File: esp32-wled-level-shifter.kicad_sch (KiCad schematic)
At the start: 5 parts, among them J1 Conn_01x04_Female, J2 Conn_01x15_Female, J3 Conn_01x15_Female, U1 CD40106

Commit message: Dimension and size tweaks
- Correctly space connectors
- Increase size of mounting holes, allow M3
- Chamfer board edges
- More silkscreen markings
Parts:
- C1: LCSC (none) -> C14663
- U1: LCSC (none) -> C38184
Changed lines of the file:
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@@
+      (effects (font (size 1.27 1.27)) hide)
+    )
+    (property "LCSC" "C38184" (id 4) (at 34.29 151.13 0)
       (effects (font (size 1.27 1.27)) hide)
     )
@@
       (effects (font (size 1.27 1.27)) hide)
     )
+    (property "LCSC" "C38184" (id 4) (at 34.29 151.13 0)
+      (effects (font (size 1.27 1.27)) hide)
+    )
     (pin "1")
     (pin "2")
@@
       (effects (font (size 1.27 1.27)) hide)
     )
+    (property "LCSC" "C38184" (id 4) (at 34.29 151.13 0)
+      (effects (font (size 1.27 1.27)) hide)
+    )
     (pin "1")
     (pin "2")
@@
     )
     (property "Datasheet" "https://assets.nexperia.com/documents/data-sheet/HEF40106B.pdf" (id 3) (at 34.29 151.13 0)
+      (effects (font (size 1.27 1.27)) hide)
+    )
+    (property "LCSC" "C38184" (id 4) (at 34.29 151.13 0)
       (effects (font (size 1.27 1.27)) hide)
     )
@@
       (effects (font (size 1.27 1.27)) hide)
     )
+    (property "LCSC" "C38184" (id 4) (at 34.29 151.13 0)
+      (effects (font (size 1.27 1.27)) hide)
+    )
     (pin "1")
     (pin "2")
@@
     )
     (property "Datasheet" "https://assets.nexperia.com/documents/data-sheet/HEF40106B.pdf" (id 3) (at 104.14 45.72 0)
+      (effects (font (size 1.27 1.27)) hide)
+    )
+    (property "LCSC" "C38184" (id 4) (at 34.29 151.13 0)
       (effects (font (size 1.27 1.27)) hide)
     )
@@
       (effects (font (size 1.27 1.27)) hide)
     )
-    (property "LCSC" "" (id 4) (at 54.61 152.4 0)
+    (property "LCSC" "C14663 " (id 4) (at 54.61 152.4 0)
       (effects (font (size 1.27 1.27)) hide)
     )
@@
       (effects (font (size 1.27 1.27)) hide)
     )
+    (property "LCSC" "C38184" (id 4) (at 34.29 151.13 0)
+      (effects (font (size 1.27 1.27)) hide)
+    )

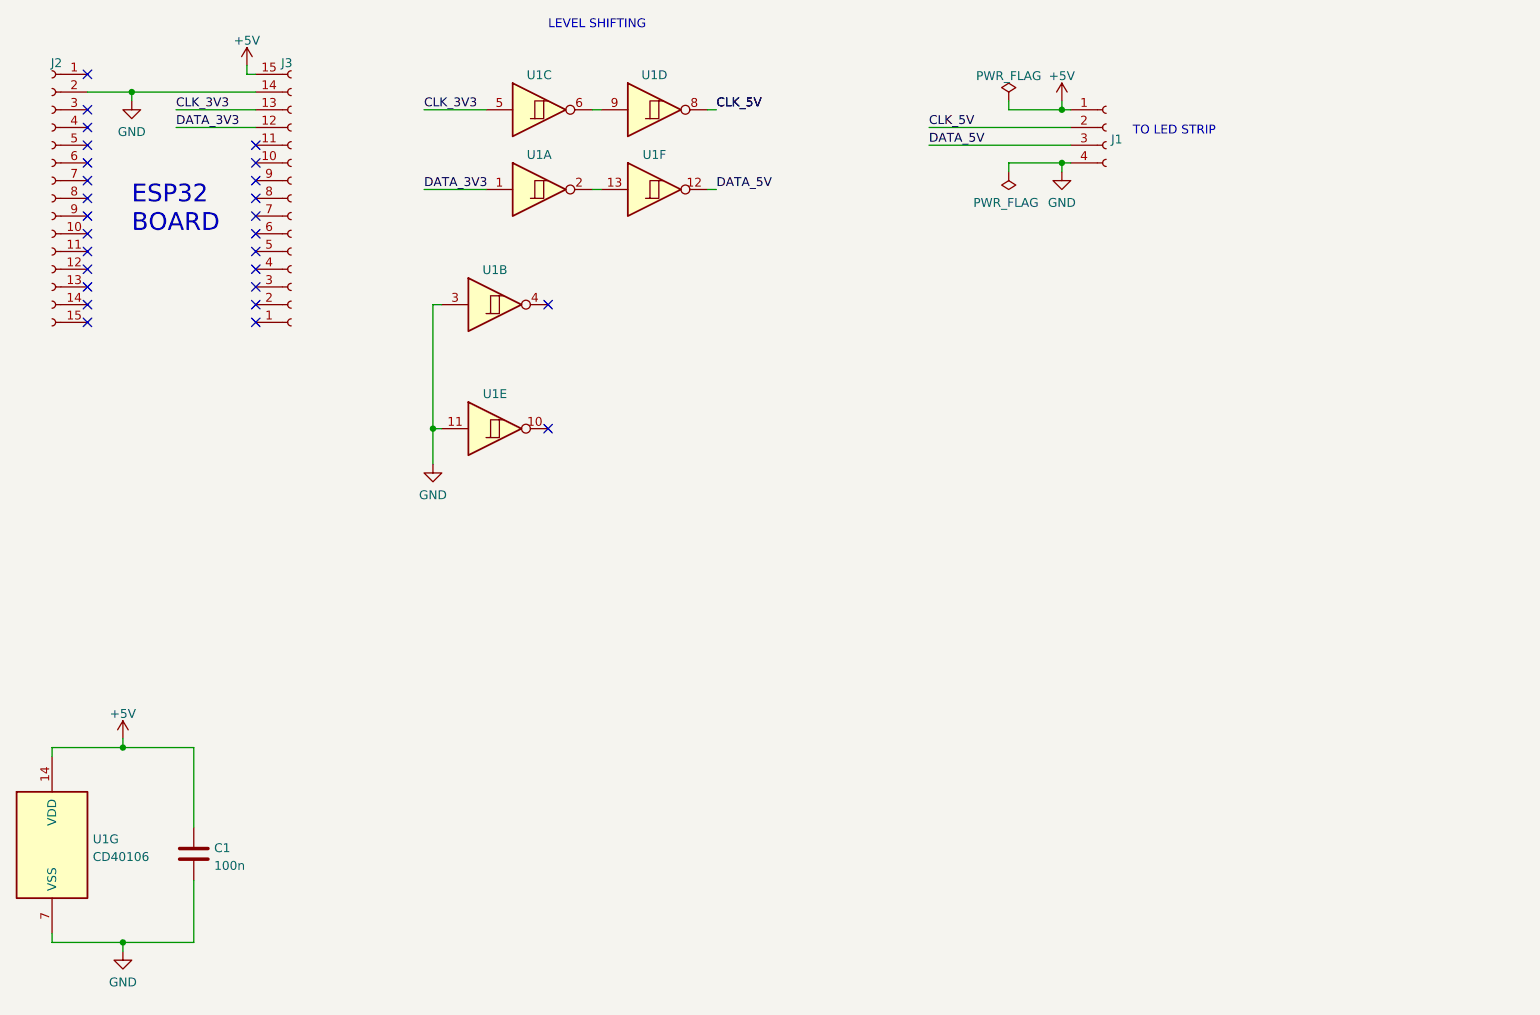
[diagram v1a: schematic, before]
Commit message: Rev2 board with experimenting playground
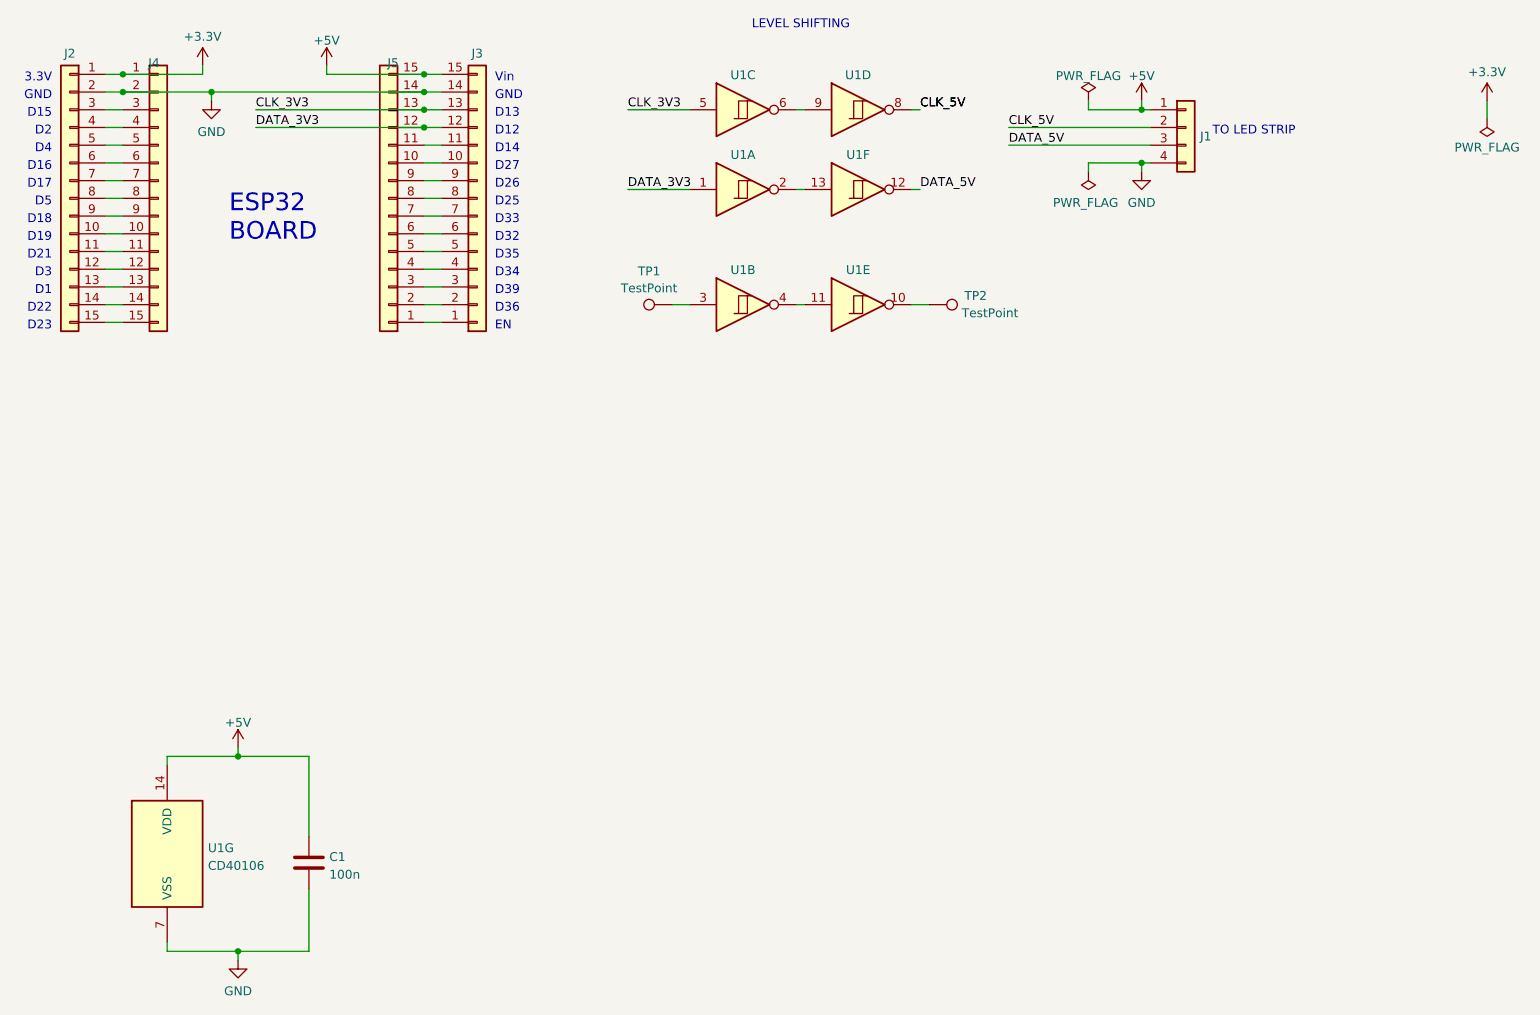
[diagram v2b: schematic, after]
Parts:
- added J4, J5: Conn_01x15_Female, Connector_PinSocket_2.54mm:PinSocket_1x15_P2.54mm_Vertical, symbol Connector_Generic:Conn_01x15
- added TP1, TP2: TestPoint, TestPoint:TestPoint_THTPad_D2.0mm_Drill1.0mm, symbol Connector:TestPoint
- J1: symbol Connector:Conn_01x04_Female -> Connector_Generic:Conn_01x04
- J2, J3: symbol Connector:Conn_01x15_Female -> Connector_Generic:Conn_01x15
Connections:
- net +5V: now also J5.15 (Pin_15)
- net CLK_3V3: now also J5.13 (Pin_13)
- net DATA_3V3: now also J5.12 (Pin_12)
- net GND: now also J4.2 (Pin_2), J5.14 (Pin_14); no longer U1.11, U1.3
- net at U1.10: now also TP2.1
- net at U1.4: now also U1.11
- net at J3.1 (Pin_1): now also J5.1 (Pin_1)
- net at J3.10 (Pin_10): now also J5.10 (Pin_10)
- net at J3.11 (Pin_11): now also J5.11 (Pin_11)
- net at J3.2 (Pin_2): now also J5.2 (Pin_2)
- net at J3.3 (Pin_3): now also J5.3 (Pin_3)
- net at J3.4 (Pin_4): now also J5.4 (Pin_4)
- net at J3.5 (Pin_5): now also J5.5 (Pin_5)
- net at J3.6 (Pin_6): now also J5.6 (Pin_6)
- net at J3.7 (Pin_7): now also J5.7 (Pin_7)
- net at J3.8 (Pin_8): now also J5.8 (Pin_8)
- net at J3.9 (Pin_9): now also J5.9 (Pin_9)
- net +3.3V: now reaches J2.1 (Pin_1)
- net +3.3V: now also J4.1 (Pin_1)
- net at J2.10 (Pin_10): now also J4.10 (Pin_10)
- net at J2.11 (Pin_11): now also J4.11 (Pin_11)
- net at J2.12 (Pin_12): now also J4.12 (Pin_12)
- net at J2.13 (Pin_13): now also J4.13 (Pin_13)
- net at J2.14 (Pin_14): now also J4.14 (Pin_14)
- net at J2.15 (Pin_15): now also J4.15 (Pin_15)
- net at J2.3 (Pin_3): now also J4.3 (Pin_3)
- net at J2.4 (Pin_4): now also J4.4 (Pin_4)
- net at J2.5 (Pin_5): now also J4.5 (Pin_5)
- net at J2.6 (Pin_6): now also J4.6 (Pin_6)
- net at J2.7 (Pin_7): now also J4.7 (Pin_7)
- net at J2.8 (Pin_8): now also J4.8 (Pin_8)
- net at J2.9 (Pin_9): now also J4.9 (Pin_9)
- new net: TP1.1, U1.3
- no-connect marks 27 -> 0
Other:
- note added: "3.3V"
- note added: "D1"
- note added: "D12"
- note added: "D13"
- note added: "D14"
- note added: "D15"
- note added: "D16"
- note added: "D17"
- note added: "D18"
- note added: "D19"
- note added: "D2"
- note added: "D21"
- note added: "D22"
- note added: "D23"
- note added: "D25"
- note added: "D26"
- note added: "D27"
- note added: "D3"
- note added: "D32"
- note added: "D33"
- note added: "D34"
- note added: "D35"
- note added: "D36"
- note added: "D39"
- note added: "D4"
- note added: "D5"
- note added: "EN"
- note added: "GND"
- note added: "Vin"
- company: (none) -> MichD
- title: (none) -> ESP32 WLED Level Shifter
- moved on the sheet: C1, U1A, U1B, U1C, U1D, U1E, U1F, U1G
